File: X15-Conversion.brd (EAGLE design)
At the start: 160 x 100 mm, 27 parts, among them U2 LINEAR,AZ1117CR-3.3TRG1DIODES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

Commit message: Fixed a lot of errors and debugged
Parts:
- removed U2: LINEAR,AZ1117CR-3.3TRG1DIODES_AZ1117CH-3.3TRG1_0_0, X15-Conversion:LINEAR,AZ1117CR-3.3TRG1
- added U1: LINEAR,AZ1117CR-3.3TRG1DIODES_AZ1117CH-3.3TRG1_0_0, X15-Conversion:LINEAR,AZ1117CR-3.3TRG1
- CIN1: device SparkFun-Capacitors:CPOL-RADIAL-5MM-10MM-KIT -> EEEFKE181XSP:CAP_EEEFKE181XSP
- moved CIN1 91.6 mm to (-62.2, -81.3)
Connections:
- net 12V: now also CIN1.1; no longer CIN1.+
- net 3.3V: now also U1.2; no longer U2.2
- net 5.2V: now also U1.3; no longer U2.3
- net GND: now also CIN1.2, U1.1, U1.4; no longer CIN1.-, U2.1

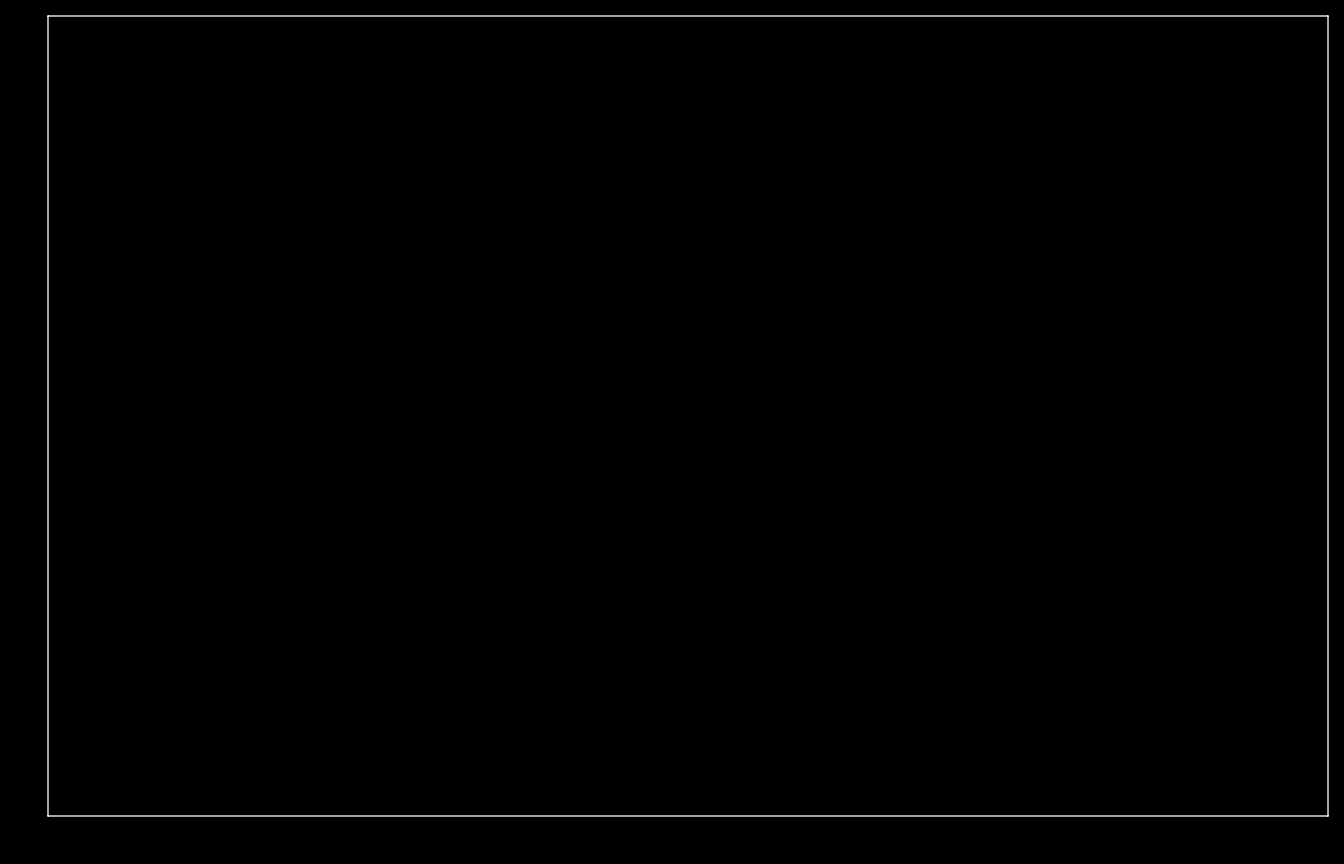
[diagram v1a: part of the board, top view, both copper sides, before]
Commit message: Revert "Revert "Merge branch 'master' of https://github.com/purduerov/X15-Conversion""
This reverts commit 3946a35888136fdb14d8eaf85822cd7069644279.
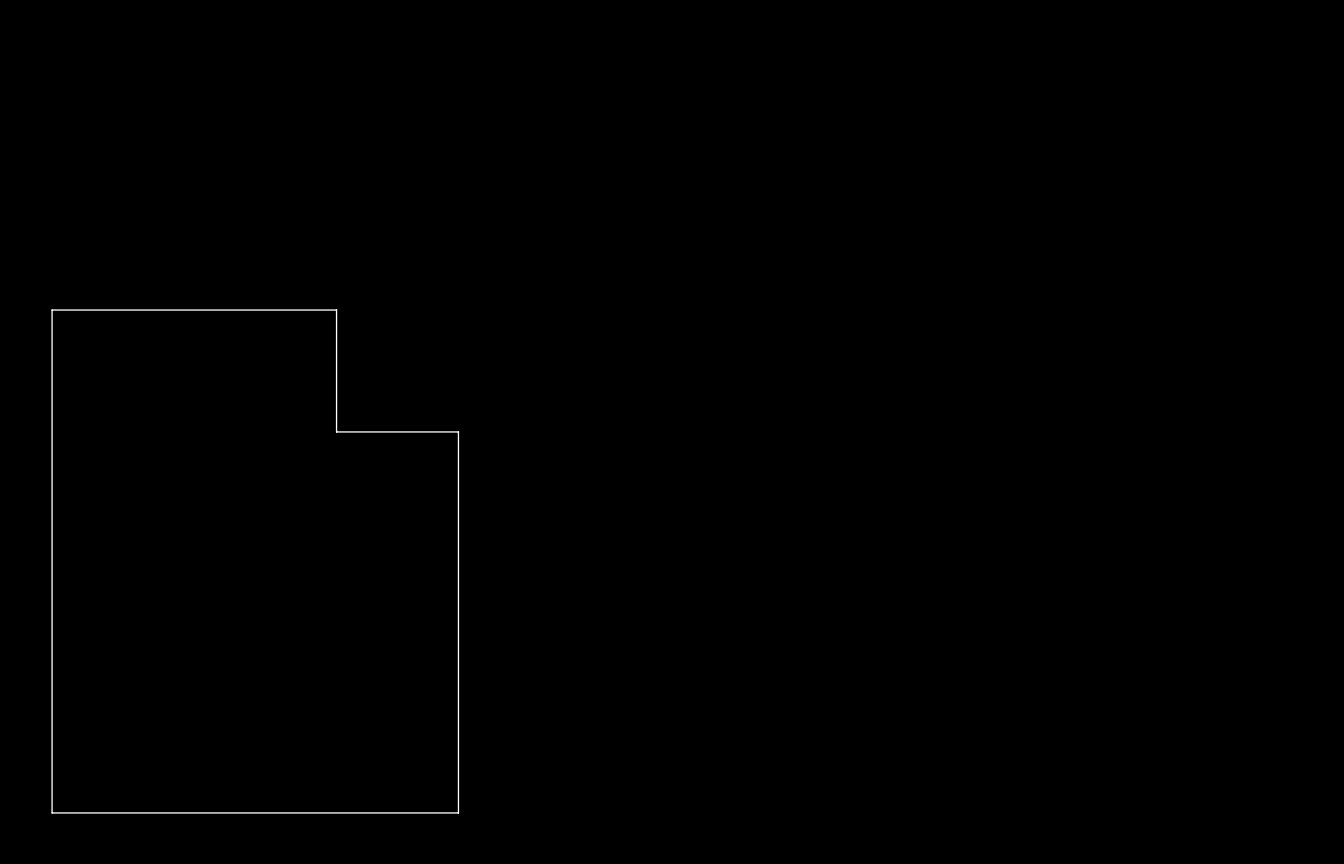
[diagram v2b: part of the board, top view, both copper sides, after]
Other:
- board size 160 x 100 mm -> 50.8 x 62.9 mm
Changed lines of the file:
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@@
 <board>
 <plain>
-<wire x1="0" y1="0" x2="160" y2="0" width="0" layer="20"/>
-<wire x1="160" y1="0" x2="160" y2="100" width="0" layer="20"/>
-<wire x1="160" y1="100" x2="0" y2="100" width="0" layer="20"/>
-<wire x1="0" y1="100" x2="0" y2="0" width="0" layer="20"/>
+<wire x1="0.508" y1="0.381" x2="51.308" y2="0.381" width="0" layer="20"/>
+<wire x1="51.308" y1="0.381" x2="51.308" y2="48.006" width="0" layer="20"/>
+<wire x1="36.068" y1="63.246" x2="0.508" y2="63.246" width="0" layer="20"/>
+<wire x1="0.508" y1="63.246" x2="0.508" y2="0.381" width="0" layer="20"/>
+<wire x1="36.068" y1="63.246" x2="36.068" y2="48.006" width="0" layer="20"/>
+<wire x1="36.068" y1="48.006" x2="51.308" y2="48.006" width="0" layer="20"/>
 </plain>
 <attributes>

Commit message: Revert "Merge branch 'master' of https://github.com/purduerov/X15-Conversion"
This reverts commit 41817e178b7c3d64232767e30bfff53a28a489f7, reversing
changes made to 9f5667108a341ebdd134b7c2334aa0d8aa0ab67e.
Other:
- board size 50.8 x 62.9 mm -> 160 x 100 mm
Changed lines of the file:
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@@
 <board>
 <plain>
-<wire x1="0.508" y1="0.381" x2="51.308" y2="0.381" width="0" layer="20"/>
-<wire x1="51.308" y1="0.381" x2="51.308" y2="48.006" width="0" layer="20"/>
-<wire x1="36.068" y1="63.246" x2="0.508" y2="63.246" width="0" layer="20"/>
-<wire x1="0.508" y1="63.246" x2="0.508" y2="0.381" width="0" layer="20"/>
-<wire x1="36.068" y1="63.246" x2="36.068" y2="48.006" width="0" layer="20"/>
-<wire x1="36.068" y1="48.006" x2="51.308" y2="48.006" width="0" layer="20"/>
+<wire x1="0" y1="0" x2="160" y2="0" width="0" layer="20"/>
+<wire x1="160" y1="0" x2="160" y2="100" width="0" layer="20"/>
+<wire x1="160" y1="100" x2="0" y2="100" width="0" layer="20"/>
+<wire x1="0" y1="100" x2="0" y2="0" width="0" layer="20"/>
 </plain>
 <attributes>
